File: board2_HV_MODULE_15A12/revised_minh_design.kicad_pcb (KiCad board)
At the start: 2 copper layers, 100 x 56.6 mm, 25 parts, among them J1 Conn_01x07_Male, J2 Conn_01x01_Male, J3 Conn_01x02_Male, U1 LM7805_TO220, U2 NE5532, U4 15A12

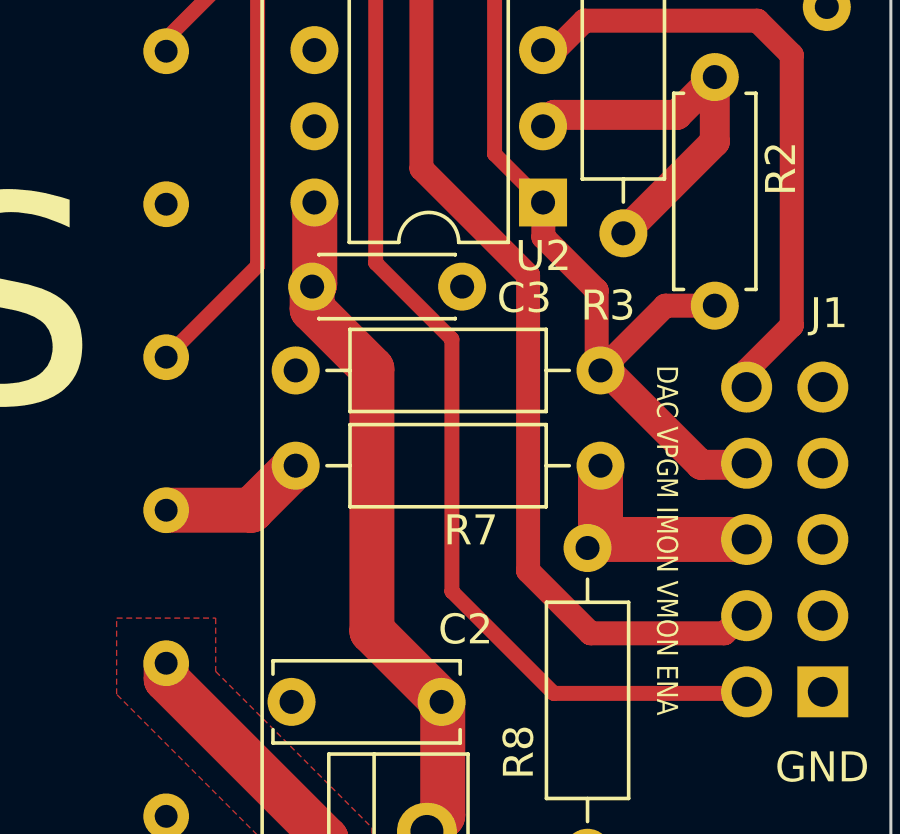
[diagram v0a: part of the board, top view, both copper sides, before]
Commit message: Fixed PI PO, DAC port ordering, MDAT Pin, clock connection
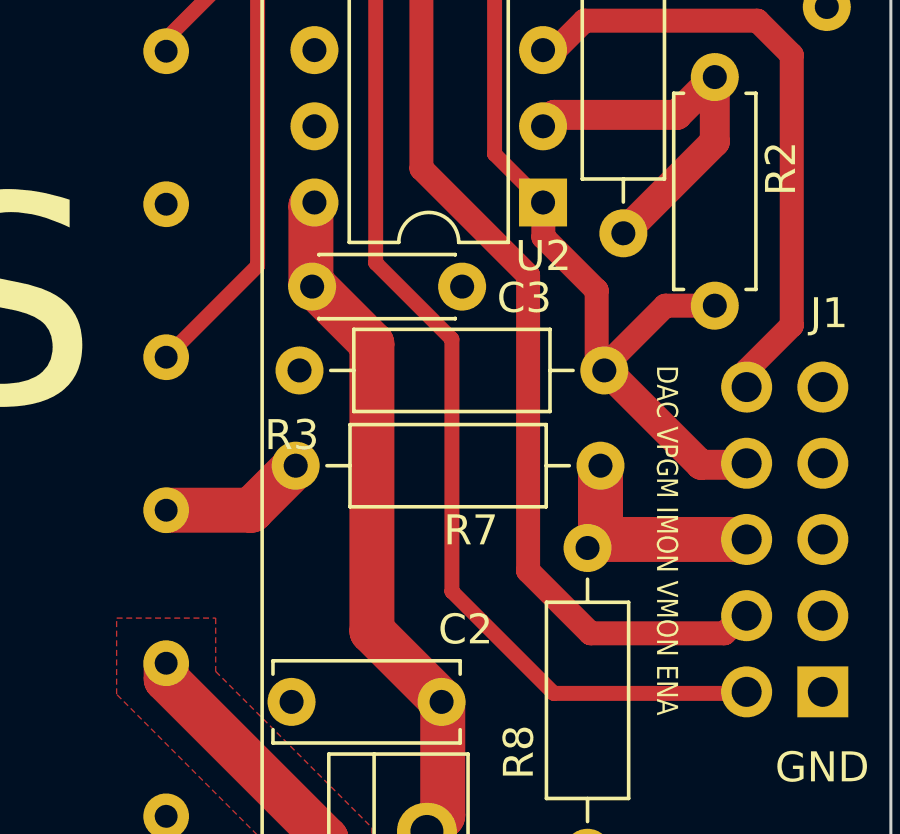
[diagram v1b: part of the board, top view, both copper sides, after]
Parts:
- R1: value 10k -> 4.7k
- R2: value 4.7k -> 2k
- R5, R7: value 2K -> 3.9K
- moved R3 10.3 mm to (180.8, 53.7), turned to 180 degrees
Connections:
- R3 pad 1: SGND -> VPGM
- R3 pad 2: VPGM -> SGND
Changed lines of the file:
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@@
       (effects (font (size 1 1) (thickness 0.15)))
     )
-    (fp_text value "10k" (at 5.08 2.37 90) (layer "F.Fab")
+    (fp_text value "4.7k" (at 5.08 2.37 90) (layer "F.Fab")
       (effects (font (size 1 1) (thickness 0.15)))
     )
@@
       (effects (font (size 1 1) (thickness 0.15)))
     )
-    (fp_text value "2K" (at 5.08 2.37) (layer "F.Fab")
+    (fp_text value "3.9K" (at 5.08 2.37) (layer "F.Fab")
       (effects (font (size 1 1) (thickness 0.15)))
     )
@@
       (effects (font (size 1 1) (thickness 0.15)))
     )
-    (fp_text value "2K" (at 5.08 2.37 90) (layer "F.Fab")
+    (fp_text value "3.9K" (at 5.08 2.37 90) (layer "F.Fab")
       (effects (font (size 1 1) (thickness 0.15)))
     )
@@
   )
   (footprint "Resistor_THT:R_Axial_DIN0207_L6.3mm_D2.5mm_P10.16mm_Horizontal" (layer "F.Cu")
-    (at 170.561 53.721)
+    (at 180.848 53.721 180)
     (descr "Resistor, Axial_DIN0207 series, Axial, Horizontal, pin pitch=10.16mm, 0.25W = 1/4W, length*diameter=6.3*2.5mm^2, http://cdn-reichelt.de/documents/datenblatt/B400/1_4W%23YAG.pdf")
     (tags "Resistor Axial_DIN0207 series Axial Horizontal pin pitch 10.16mm 0.25W = 1/4W length 6.3mm diameter 2.5mm")
@@
     (fp_line (start 1.93 1.25) (end 8.23 1.25) (layer "F.Fab") (width 0.1))
     (fp_line (start 8.23 -1.25) (end 1.93 -1.25) (layer "F.Fab") (width 0.1))
-    (pad "1" thru_hole circle (at 0 0) (size 1.6 1.6) (drill 0.8) (layers *.Cu *.Mask)
+    (pad "1" thru_hole circle (at 0 0 180) (size 1.6 1.6) (drill 0.8) (layers *.Cu *.Mask)
+      (net 5 "VPGM") (pintype "passive"))
+    (pad "2" thru_hole oval (at 10.16 0 180) (size 1.6 1.6) (drill 0.8) (layers *.Cu *.Mask)
       (net 17 "SGND") (pintype "passive"))
-    (pad "2" thru_hole oval (at 10.16 0) (size 1.6 1.6) (drill 0.8) (layers *.Cu *.Mask)
-      (net 5 "VPGM") (pintype "passive"))
     (model "${KICAD6_3DMODEL_DIR}/Resistor_THT.3dshapes/R_Axial_DIN0207_L6.3mm_D2.5mm_P10.16mm_Horizontal.wrl"
       (offset (xyz 0 0 0))
@@
       (effects (font (size 1 1) (thickness 0.15)))
     )
-    (fp_text value "4.7k" (at 3.81 2.37 -90) (layer "F.Fab")
+    (fp_text value "2k" (at 3.81 2.37 -90) (layer "F.Fab")
       (effects (font (size 1 1) (thickness 0.15)))
     )
@@
     (property "Sheetfile" "revised_minh_design.kicad_sch")
     (property "Sheetname" "")
-    (attr exclude_from_pos_files)
+    (property "exclude_from_bom" "")
+    (attr exclude_from_pos_files exclude_from_bom)
     (fp_text reference "J2" (at 0 2.47 90) (layer "B.SilkS")
       (effects (font (size 1 1) (thickness 0.15)) (justify mirror))
@@
   (segment (start 180.771911 76.987511) (end 181.7116 77.9272) (width 1.5) (layer "F.Cu") (net 1))
   (segment (start 171.577 74.168) (end 174.935 74.168) (width 1.5) (layer "F.Cu") (net 1))
-  (segment (start 171.196 50.84) (end 171.109 50.927) (width 1.5) (layer "F.Cu") (net 2))
+  (segment (start 171.186 48.123) (end 171.069 48.24) (width 1.5) (layer "F.Cu") (net 2))
   (segment (start 175.4632 64.77) (end 175.4632 68.5598) (width 1.5) (layer "F.Cu") (net 2))
-  (segment (start 171.109 50.927) (end 171.109 51.6782) (width 1.5) (layer "F.Cu") (net 2))
   (segment (start 173.101 62.4078) (end 175.4632 64.77) (width 1.5) (layer "F.Cu") (net 2))
-  (segment (start 171.109 51.6782) (end 173.101 53.6702) (width 1.5) (layer "F.Cu") (net 2))
-  (segment (start 173.101 53.6702) (end 173.101 62.4078) (width 1.5) (layer "F.Cu") (net 2))
+  (segment (start 171.109 50.927) (end 171.196 50.927) (width 1.5) (layer "F.Cu") (net 2))
+  (segment (start 173.101 52.832) (end 173.101 62.4078) (width 1.5) (layer "F.Cu") (net 2))
+  (segment (start 171.196 50.927) (end 173.101 52.832) (width 1.5) (layer "F.Cu") (net 2))
   (segment (start 175.4632 68.5598) (end 174.935 69.088) (width 1.5) (layer "F.Cu") (net 2))
-  (segment (start 171.196 48.133) (end 171.196 50.84) (width 1.5) (layer "F.Cu") (net 2))
-  (segment (start 171.186 48.123) (end 171.196 48.133) (width 1.5) (layer "F.Cu") (net 2))
+  (segment (start 171.069 50.887) (end 171.109 50.927) (width 1.5) (layer "F.Cu") (net 2))
+  (segment (start 171.069 48.24) (end 171.069 50.887) (width 1.5) (layer "F.Cu") (net 2))
   (segment (start 185.2676 33.9394) (end 185.3134 33.9852) (width 1) (layer "F.Cu") (net 3))
   (segment (start 185.3134 33.9852) (end 188.2648 33.9852) (width 1) (layer "F.Cu") (net 3))
